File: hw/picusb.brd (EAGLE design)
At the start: 45.7 x 33.3 mm, 38 parts, among them Q1 BSS138, Q2 BSS138, Q3 BSS84, Q4 BSS84, U1 PIC16F1454SOIC, U2 AP7115W, X1 MINI-USB-UX60-MB-5ST

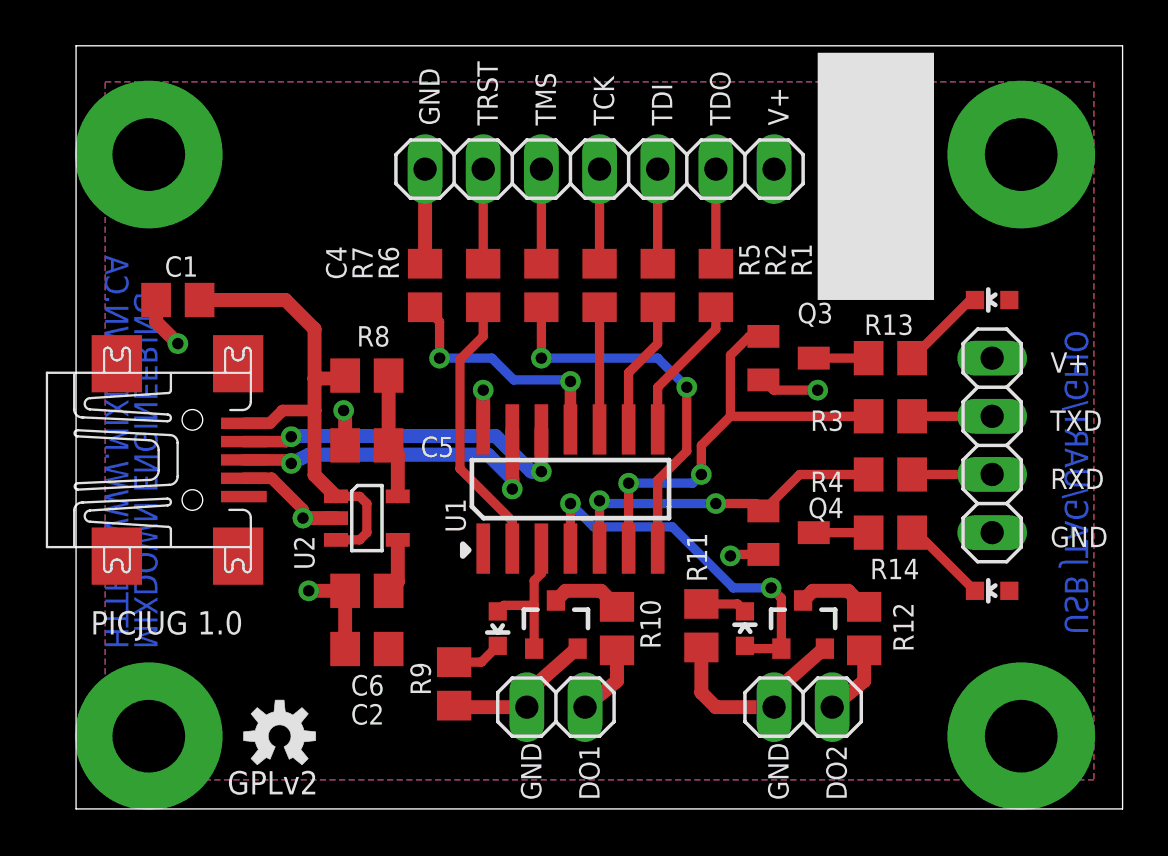
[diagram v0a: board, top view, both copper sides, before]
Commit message: use 0805 LEDs
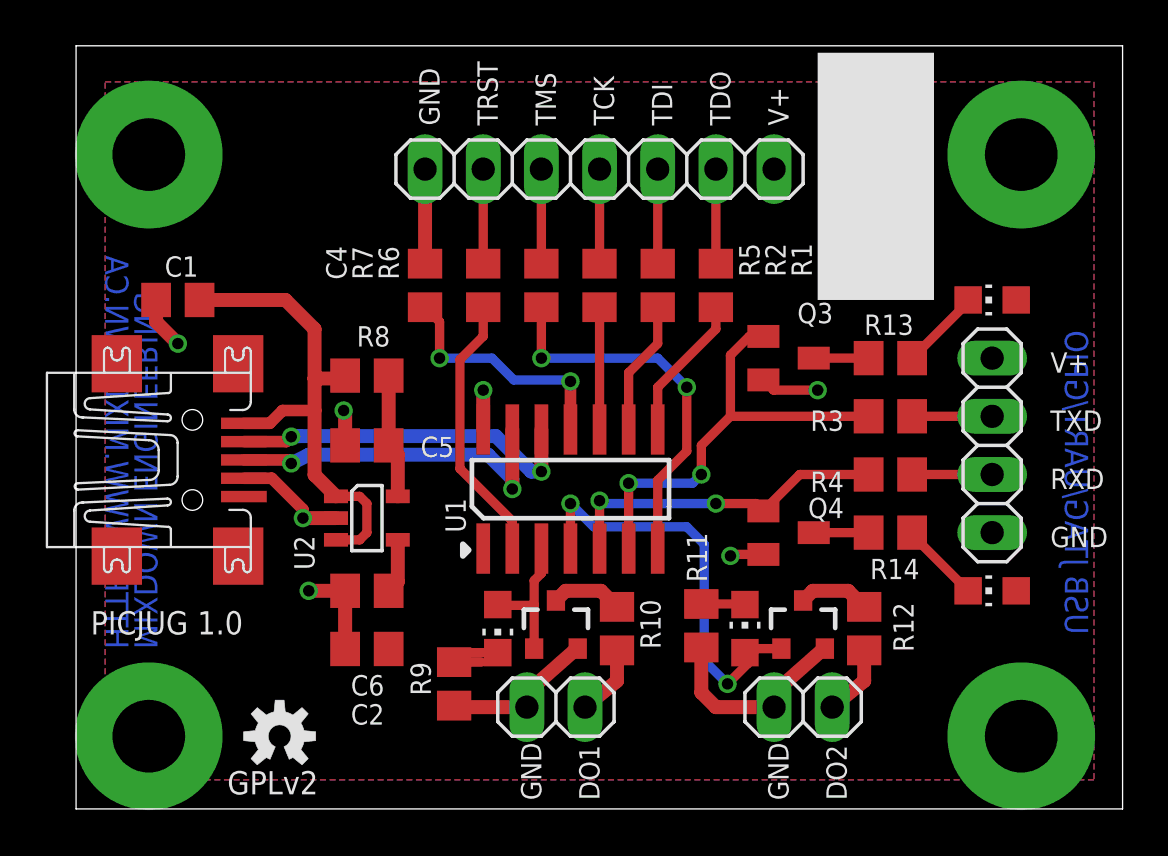
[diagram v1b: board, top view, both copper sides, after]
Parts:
- removed D1, D2, D3, D4: (no value), SparkFun:LED-0603
- added LED1, LED2, LED3, LED4: (no value), led:CHIP-LED0805
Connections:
- net DO1: now also LED1.A; no longer D1.A
- net DO2: now also LED2.A; no longer D2.A
- net N$14: now also LED3.C; no longer D3.C
- net N$17: now also LED2.C; no longer D2.C
- net N$18: now also LED4.C; no longer D4.C
- net N$8: now also LED1.C; no longer D1.C
- net V+: now also LED3.A, LED4.A; no longer D3.A, D4.A
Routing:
- net DO2: track 16.7 -> 19.0 mm
- net N$8: track 2.20 -> 3.51 mm

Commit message: minor edits to board overall dimensions and text
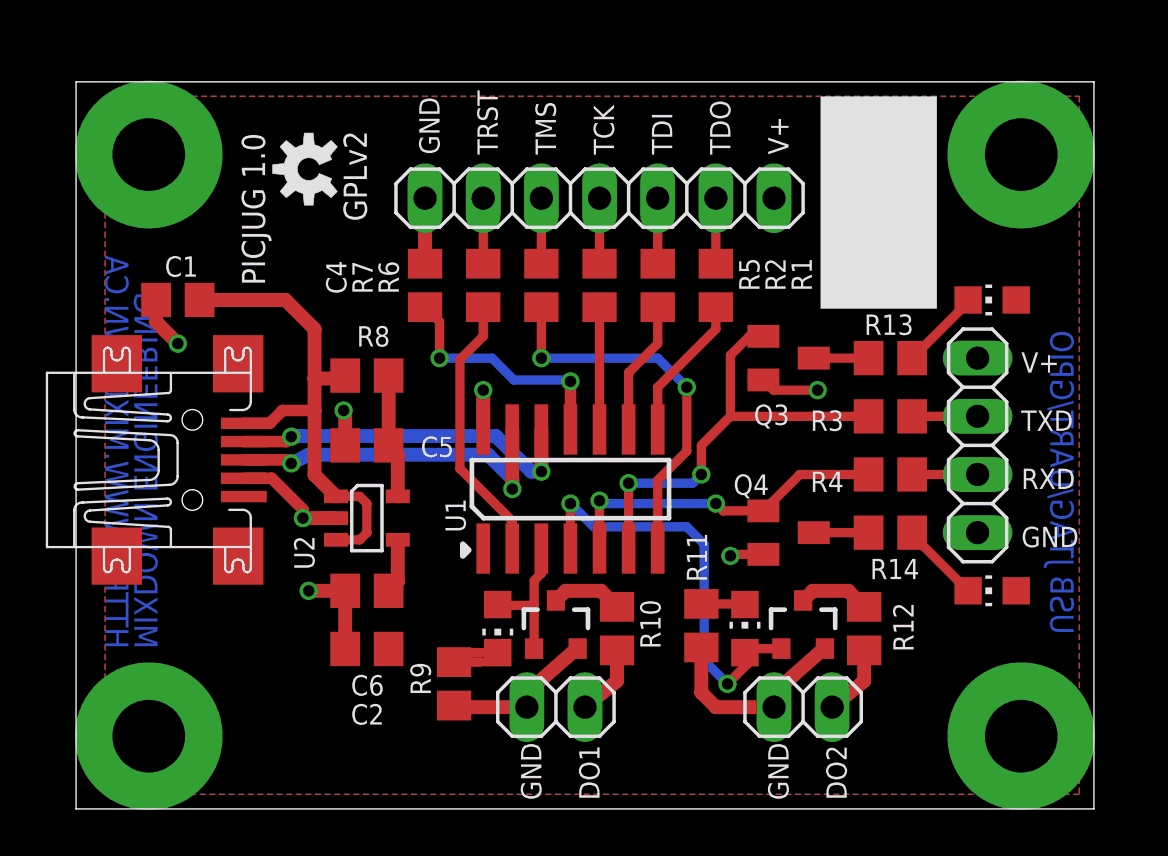
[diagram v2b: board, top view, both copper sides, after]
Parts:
- moved JP3 1.27 mm to (22.9, 26.7)
- moved JP1 0.64 mm to (39.4, 15.9)
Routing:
- net N$9: track 4.13 -> 2.86 mm
- net N$7: track 4.13 -> 2.86 mm
- net N$3: track 4.13 -> 2.86 mm
- net N$11: track 4.13 -> 2.86 mm
- net N$10: track 4.13 -> 2.86 mm
- net GND: track 38.6 -> 37.3 mm
- net N$6: track 3.50 -> 2.86 mm
- net N$5: track 3.50 -> 2.86 mm
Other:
- board size 45.7 x 33.3 mm -> 44.5 x 31.8 mm
